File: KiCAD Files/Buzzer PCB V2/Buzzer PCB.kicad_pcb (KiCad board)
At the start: 2 copper layers, 90 x 50 mm, 18 parts, among them J1 2600mAh LiPo JST-PH bottom, J10 Adafruit ESP32 Feather V2 hea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, J11 OLED FeatherWing header, J2 Legacy SW_BAT/GND out, J3 SD card module, swapped pins, J4 Legacy D13 test pad, J5 GPS M100 Mini, J6 BMP390/BMP5xx top module, J7 SHT41 top module, Q1 S8050, SW1 SS12D00G5, U1 TP4057 USB-C charger

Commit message: V2 with sparkfun
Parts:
- added SW2: BACK, Vario_Buzzer_V2:Ant_Display_SW_PUSH_6mm_H5mm, F.Cu at (4.00, 41.0)
- added SW3: NEXT, Vario_Buzzer_V2:Ant_Display_SW_PUSH_6mm_H5mm, F.Cu at (14.0, 41.0)
- added SW4: DOWN, Vario_Buzzer_V2:Ant_Display_SW_PUSH_6mm_H5mm, F.Cu at (24.0, 41.0)
- added SW5: UP, Vario_Buzzer_V2:Ant_Display_SW_PUSH_6mm_H5mm, F.Cu at (38.0, 41.0)
- J10: value Adafruit ESP32 Feather V2 header -> SparkFun Thing Plus ESP32 WROOM-C USB-C header; footprint Vario_Buzzer_V2:Feather_28_Header_Separate -> Vario_Buzzer_V2:SparkFun_Thing_Plus_ESP32_WROOM_C_Header
- J11: value OLED FeatherWing header -> SparkFun Qwiic OLED 1.3in module; footprint Vario_Buzzer_V2:OLED_FeatherWing_28_Header -> Vario_Buzzer_V2:SparkFun_Qwiic_OLED_1p3_Module
- J3: value SD card module, swapped pins -> Optional external SD module; Thing Plus has onboard microSD
- J5: value GPS M100 Mini -> HGLRC M100 Mini GPS manual pinout
- J6: value BMP390/BMP5xx top module -> BMP390/BMP5xx top pads
- J7: value SHT41 top module -> SHT41 top pads
- moved U1 72.0 mm to (10.5, 6.80), turned to 180 degrees
- moved C2 40.7 mm to (18.2, 9.50)
- moved C1 36.0 mm to (22.5, 4.20)
- moved SW1 32.5 mm to (25.0, 12.0)
- moved J10 32.0 mm to (60.0, 13.0)
- moved J4 17.9 mm to (68.0, 15.0)
- moved BZ1 17.5 mm to (85.0, 13.0)
- moved J7 15.3 mm to (81.0, 37.0), turned to 90 degrees
- moved J5 15.3 mm to (72.0, 41.5)
- moved J3 12.9 mm to (52.0, 31.0)
- moved J11 11.4 mm to (18.0, 31.6)
- moved R1 10.7 mm to (70.5, 15.0)
- moved J6 7.94 mm to (61.0, 35.0)
- moved R2 5.73 mm to (74.0, 15.0)
- moved Q1 4.92 mm to (78.0, 15.0)
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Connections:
- J10 pad 1: RESET -> SDA
- J10 pad 11: SPI_SCK -> (no net)
- J10 pad 12: SPI_MOSI -> SW_BAT
- J10 pad 13: SPI_MISO -> BTN_UP_GPIO21
- J10 pad 14: GPS_TX_FEATHER_RX -> GPS_RX_THING_TX
- J10 pad 15: GPS_RX_FEATHER_TX -> GPS_TX_THING_RX
- J10 pad 16: (no net) -> SPI_MISO
- J10 pad 17: SDA -> SPI_MOSI
- J10 pad 18: SCL -> SPI_SCK
- J10 pad 19: D5_IO14_BTN_C -> (no net)
- J10 pad 2: 3V3 -> SCL
- J10 pad 20: D6_IO32_BTN_B -> (no net)
- J10 pad 21: D9_IO15_BTN_A -> (no net)
- J10 pad 22: SD_CS_D10_IO27 -> (no net)
- J10 pad 25: D13 -> GND
- J10 pad 27: (no net) -> 3V3
- J10 pad 28: SW_BAT -> (no net)
- J10 pad 4: GND -> BTN_DOWN_GPIO5
- J10 pad 5: (no net) -> BTN_NEXT_GPIO4
- J10 pad 6: (no net) -> BTN_BACK_GPIO3
- J10 pad 7: (no net) -> SD_CS_GPIO2
- J10 pad 9: (no net) -> D13_BUZZER_GPIO13
- J11 pad 1: RESET -> GND
- J11 pad 3: (no net) -> SDA
- J11 pad 4: GND -> SCL
- J3 pad 5: SD_CS_D10_IO27 -> SD_CS_GPIO2
- J4 pad e: D13 -> D13_BUZZER_GPIO13
- J5 pad 1: GND -> GPS_RX_THING_TX
- J5 pad 2: 3V3 -> GPS_TX_THING_RX
- J5 pad 3: GPS_TX_FEATHER_RX -> 3V3
- J5 pad 4: GPS_RX_FEATHER_TX -> GND
- R1 pad 1: D13 -> D13_BUZZER_GPIO13
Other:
- board text added: "BTN nets copied from Ant Display: BACK GPIO3, NEXT GPIO4, DOWN GPIO5, UP net on FREEBIE/ESP4"
- board text added: "Back side: optional external SD plus HGLRC M100"
- board text added: "C1 bulk, C2 decoupling on SW_BAT/GND"
- board text added: "J1 bottom LiPo JST"
- board text added: "J10 SparkFun Thing Plus ESP32 WROOM-C, SparkFun Eagle header geometry"
- board text added: "J11 SparkFun Qwiic OLED 1.3in; J3 pins GND 3V3 SDA SCL"
- board text added: "J5 HGLRC M100 manual pin order: RX TX VCC GND"
- board text added: "PCB 90x50mm, 1.5mm FR4; drill set: 0.8/1/1.2/1.4/1.6/2/2.4/3/3.175mm"
- board text added: "R1 470R D13/GPIO13 to Q1 base"
- board text added: "R2 100k base to GND; Q1 S8050 E-B-C"
- board text added: "U1 USB-C edge faces board left; BAT pads face right"
- board text added: "Vario Buzzer / Sensor Interposer V2 - SparkFun Thing Plus + Qwiic OLED, no traces"
- board text removed: "Back: SD + M100"
- board text removed: "C1 47-100uF SW_BAT/GND"
- board text removed: "C2 0.1uF SW_BAT/GND"
- board text removed: "J1 bottom: LiPo JST"
- board text removed: "J10 FEATHER"
- board text removed: "J11 OLED FEATHERWING"
- board text removed: "PCB 90x50mm, 2.0mm"
- board text removed: "Q1 S8050 E-B-C"
- board text removed: "R1 470R D13 to Q1 base"
- board text removed: "R2 100k base to GND"
- board text removed: "U1 USB-C edge -> board edge"
- board text removed: "Vario Buzzer / Sensor Interposer V2 - placement only, no traces"

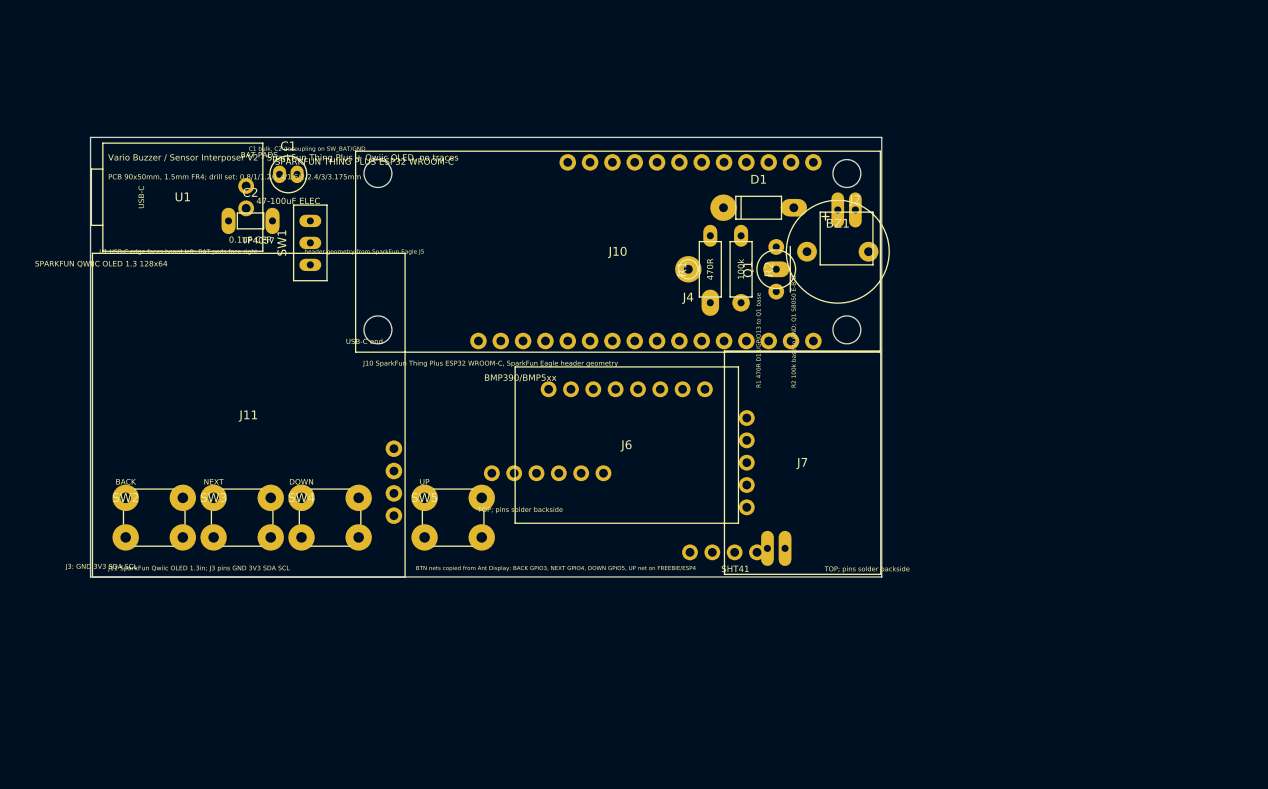
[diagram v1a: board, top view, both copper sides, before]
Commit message: Restore KiCad component references and footprints
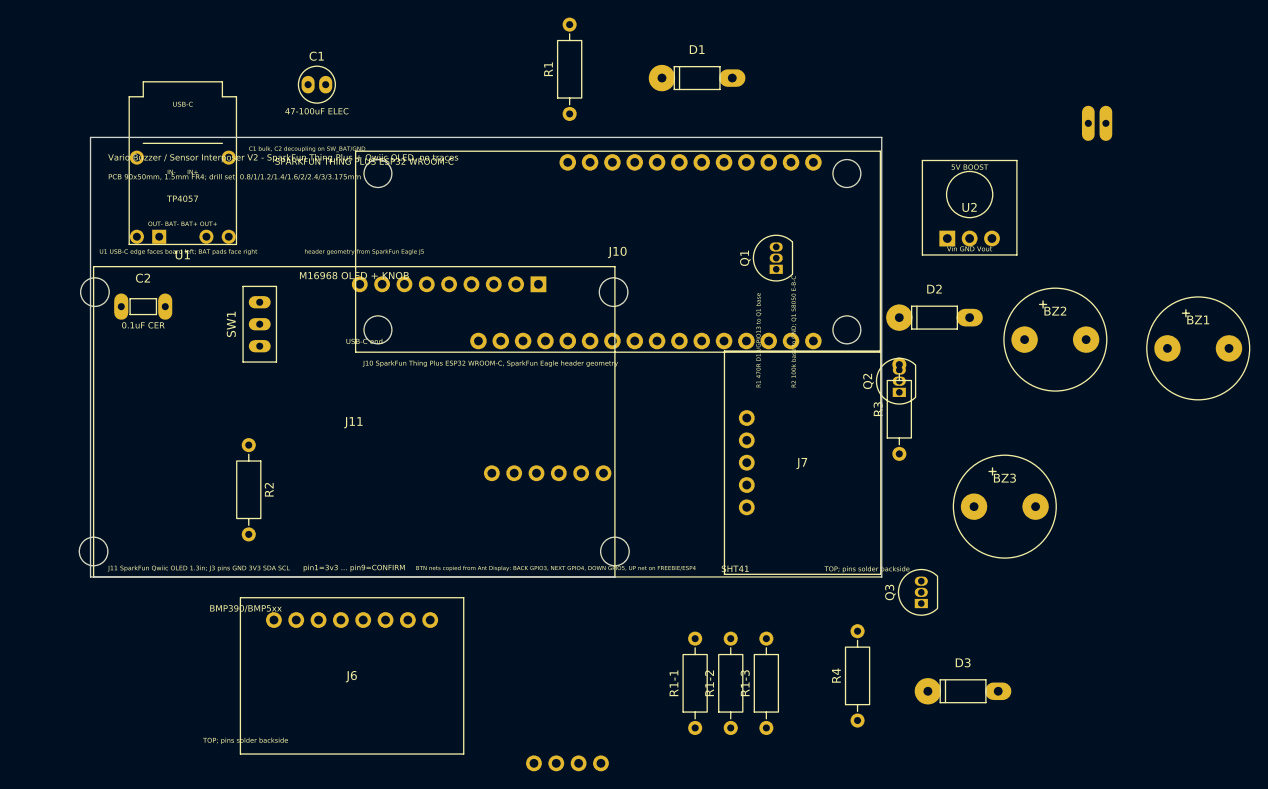
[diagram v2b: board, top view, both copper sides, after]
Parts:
- removed J2: Legacy SW_BAT/GND out, Connector_JST:JST_PH_S2B-PH-K_1x02_P2.00mm_Horizontal
- removed J4: Legacy D13 test pad, Connector_PinHeader_2.54mm:PinHeader_1x01_P2.54mm_Vertical
- removed SW2: BACK, Vario_Buzzer_V2:Ant_Display_SW_PUSH_6mm_H5mm
- removed SW3: NEXT, Vario_Buzzer_V2:Ant_Display_SW_PUSH_6mm_H5mm
- removed SW4: DOWN, Vario_Buzzer_V2:Ant_Display_SW_PUSH_6mm_H5mm
- removed SW5: UP, Vario_Buzzer_V2:Ant_Display_SW_PUSH_6mm_H5mm
- added BZ2: 12085 Passive Buzzer 42R, Buzzer_Beeper:Buzzer_12x8.5mm_P7.62mm_Custom, F.Cu at (109.8, 23.0)
- added BZ3: 12085 Passive Buzzer 42R, Buzzer_Beeper:Buzzer_12x8.5mm_P7.62mm_Custom, F.Cu at (104.0, 42.0)
- added D2: 1N5819, Diode_THT:D_DO-41_SOD81_P10.16mm_Horizontal, F.Cu at (96.0, 20.5)
- added D3: 1N5819, Diode_THT:D_DO-41_SOD81_P10.16mm_Horizontal, F.Cu at (99.2, 63.0)
- added Q2: S8050, Package_TO_SOT_THT:TO-92_Inline, F.Cu at (92.0, 29.0)
- added Q3: S8050, Package_TO_SOT_THT:TO-92_Inline, F.Cu at (94.5, 53.0)
- added R1-1: 100k, Resistor_THT:R_Axial_DIN0207_L6.3mm_D2.5mm_P10.16mm_Horizontal, F.Cu at (68.8, 67.2)
- added R1-2: 100k, Resistor_THT:R_Axial_DIN0207_L6.3mm_D2.5mm_P10.16mm_Horizontal, F.Cu at (72.8, 67.2)
- added R1-3: 100k, Resistor_THT:R_Axial_DIN0207_L6.3mm_D2.5mm_P10.16mm_Horizontal, F.Cu at (76.9, 67.2)
- added R3: 470R, Resistor_THT:R_Axial_DIN0207_L6.3mm_D2.5mm_P10.16mm_Horizontal, F.Cu at (92.0, 36.0)
- added R4: 470R, Resistor_THT:R_Axial_DIN0207_L6.3mm_D2.5mm_P10.16mm_Horizontal, F.Cu at (87.2, 66.3)
- added U2: Comidox 5V Booster, Vario_Buzzer_V2:Comidox_5V_Booster_10.75x10.75_3Pin, F.Cu at (100.0, 8.00)
- C2: footprint Capacitor_THT:C_Disc_D3.0mm_W1.6mm_P2.50mm -> Vario_Buzzer_V2:Ceramic_Cap_0.1uF_P5.00mm_V1
- J10: value SparkFun Thing Plus ESP32 WROOM-C USB-C header -> SparkFun Thing Plus ESP32 WROOM-C USB-C
- J11: value SparkFun Qwiic OLED 1.3in module -> M16968 OLED + Rotary Knob; footprint Vario_Buzzer_V2:SparkFun_Qwiic_OLED_1p3_Module -> Vario_Buzzer_V2:OLED_M16968_59x35_9Pin
- J3: value Optional external SD module; Thing Plus has onboard microSD -> Optional SD module 18x18 swapped
- J5: value HGLRC M100 Mini GPS manual pinout -> HGLRC M100 Mini GPS
- J6: value BMP390/BMP5xx top pads -> BMP581/BMP5xx top pads
- Q1: footprint Package_TO_SOT_THT:TO-92_Inline_Wide_Formed -> Package_TO_SOT_THT:TO-92_Inline
- R1: footprint Resistor_THT:R_Axial_DIN0207_L6.3mm_D2.5mm_P7.62mm_Horizontal -> Resistor_THT:R_Axial_DIN0207_L6.3mm_D2.5mm_P10.16mm_Horizontal
- R2: value 100k -> 470R; footprint Resistor_THT:R_Axial_DIN0207_L6.3mm_D2.5mm_P7.62mm_Horizontal -> Resistor_THT:R_Axial_DIN0207_L6.3mm_D2.5mm_P10.16mm_Horizontal
- SW1: value SS12D00G5 -> SS12D00G5 power switch
- U1: footprint Vario_Buzzer_V2:TP4057_Module_18.2x12.3 -> Vario_Buzzer_V2:TP4057_Module_12.2x18.5
- moved J1 60.6 mm to (114.5, -3.35)
- moved R2 59.5 mm to (18.0, 35.0)
- moved BZ1 42.4 mm to (126.0, 24.0)
- moved J6 40.8 mm to (29.8, 61.2)
- moved J5 29.9 mm to (54.2, 65.5)
- moved R1 23.8 mm to (54.5, -2.67)
- moved D1 16.3 mm to (69.0, -6.75)
- moved C2 15.6 mm to (6.00, 19.2)
- moved J11 12.0 mm to (30.0, 32.4)
- moved SW1 10.9 mm to (19.2, 21.2)
- moved C1 10.7 mm to (25.8, -6.00)
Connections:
- BZ1 pad 1: SW_BAT -> /BUZZER_LOW
- BZ1 pad 2: BUZZER_LOW -> /A
- C1 pad 1: SW_BAT -> /GND
- C1 pad 2: GND -> /SW_BAT
- C2 pad 1: SW_BAT -> /GND
- C2 pad 2: GND -> unconnected-(C2-Pad2)
- D1 pad 1: SW_BAT -> /BUZZER_LOW
- D1 pad 2: BUZZER_LOW -> /A
- J1 pad 1: BAT_IN -> /GND
- J1 pad 2: GND -> /BAT_IN
- J10 pad 1: SDA -> /SDA
- J10 pad 10: (no net) -> unconnected-(J10-V_USB-Pad10)
- J10 pad 11: (no net) -> unconnected-(J10-EN-Pad11)
- J10 pad 12: SW_BAT -> /SW_BAT
- J10 pad 13: BTN_UP_GPIO21 -> unconnected-(J10-FREEBIE/ESP4-Pad13)
- J10 pad 14: GPS_RX_THING_TX -> /GPS_RX_THING_TX
- J10 pad 15: GPS_TX_THING_RX -> /D13_BUZZER_GPIO13
- J10 pad 16: SPI_MISO -> /SPI_MISO
- J10 pad 17: SPI_MOSI -> /SPI_MOSI
- J10 pad 18: SPI_SCK -> /SPI_SCK
- J10 pad 19: (no net) -> /BTN_BACK_GPIO3
- J10 pad 2: SCL -> /SCL
- J10 pad 20: (no net) -> /BTN_NEXT_GPIO4
- J10 pad 21: (no net) -> /BTN_DOWN_GPIO5
- J10 pad 22: (no net) -> /BTN_UP_GPIO21
- J10 pad 23: (no net) -> /SD_CS_GPIO2
- J10 pad 24: (no net) -> /BUZZER2_ESP26
- J10 pad 25: GND -> /GND
- J10 pad 26: (no net) -> unconnected-(J10-AREF/NC-Pad26)
- J10 pad 27: 3V3 -> unconnected-(J10-3V3-Pad27)
- J10 pad 28: (no net) -> unconnected-(J10-RESET-Pad28)
- J10 pad 3: (no net) -> unconnected-(J10-GPIO6/ESP14-Pad3)
- J10 pad 4: BTN_DOWN_GPIO5 -> unconnected-(J10-GPIO5/ESP32-Pad4)
- J10 pad 5: BTN_NEXT_GPIO4 -> unconnected-(J10-GPIO4/ESP15-Pad5)
- J10 pad 6: BTN_BACK_GPIO3 -> unconnected-(J10-GPIO3/ESP33-Pad6)
- J10 pad 7: SD_CS_GPIO2 -> /BUZZER3_GPIO2_ESP27
- J10 pad 8: (no net) -> unconnected-(J10-GPIO1/ESP12-Pad8)
- J10 pad 9: D13_BUZZER_GPIO13 -> /GPS_TX_THING_RX
- J11 pad 1: GND -> /3V3
- J11 pad 2: 3V3 -> /GND
- J11 pad 3: SDA -> /BTN_BACK_GPIO3
- J11 pad 4: SCL -> /BTN_NEXT_GPIO4
- J3 pad 1: GND -> /3V3
- J3 pad 2: SPI_MISO -> /SD_CS_GPIO2
- J3 pad 3: SPI_SCK -> /SPI_MOSI
- J3 pad 4: SPI_MOSI -> /SPI_SCK
- J3 pad 5: SD_CS_GPIO2 -> /SPI_MISO
- J3 pad 6: 3V3 -> /GND
- J5 pad 1: GPS_RX_THING_TX -> /GND
- J5 pad 2: GPS_TX_THING_RX -> /3V3
- J5 pad 3: 3V3 -> /GPS_TX_THING_RX
- J5 pad 4: GND -> /GPS_RX_THING_TX
- J6 pad 1: 3V3 -> /3V3
- J6 pad 2: 3V3 -> /3V3
- J6 pad 3: GND -> /GND
- J6 pad 4: SCL -> /SCL
- J6 pad 5: (no net) -> unconnected-(J6-SDO/ADR-Pad5)
- J6 pad 6: SDA -> /SDA
- J6 pad 7: (no net) -> unconnected-(J6-CS-Pad7)
- J6 pad 8: (no net) -> unconnected-(J6-INT-Pad8)
- J7 pad 1: 3V3 -> /3V3
- J7 pad 2: 3V3 -> /3V3
- J7 pad 3: GND -> /GND
- J7 pad 4: SCL -> /SCL
- J7 pad 5: SDA -> /SDA
- Q1 pad 1: GND -> /BUZZER_LOW
- Q1 pad 2: BUZZER_BASE -> /BUZZER_BASE
- Q1 pad 3: BUZZER_LOW -> /GND
- R1 pad 1: D13_BUZZER_GPIO13 -> /BUZZER_BASE
- R1 pad 2: BUZZER_BASE -> /D13_BUZZER_GPIO13
- R2 pad 1: BUZZER_BASE -> /BUZZER_BASE2
- R2 pad 2: GND -> /BUZZER2_ESP26
- SW1 pad 1: SW_BAT -> /GND
- SW1 pad 2: BAT_IN -> /BAT_IN
- SW1 pad 3: (no net) -> /SW_BAT
- U1 pad 1: BAT_IN -> /GND
- U1 pad 2: GND -> /BAT_IN

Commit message: Reposition buzzer PCB footprints and add SHT41 header
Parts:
- moved R2 214.1 mm to (231.2, 54.5), turned to 180 degrees
- moved D1 192.7 mm to (259.2, 24.5)
- moved R1 180.5 mm to (231.2, 34.5), turned to 180 degrees
- moved R1-1 180.0 mm to (247.2, 43.4)
- moved R1-2 174.4 mm to (247.2, 63.4)
- moved R1-3 171.1 mm to (247.2, 83.4)
- moved D2 164.9 mm to (259.2, 44.5)
- moved Q1 161.3 mm to (238.2, 34.5)
- moved D3 159.9 mm to (259.2, 64.5)
- moved BZ3 158.5 mm to (259.2, 74.5)
- moved BZ2 152.7 mm to (259.2, 54.5)
- moved Q2 148.4 mm to (238.2, 54.5)
- moved Q3 145.3 mm to (238.2, 74.5)
- moved R4 145.1 mm to (231.2, 84.5), turned to 180 degrees
- moved R3 144.4 mm to (231.2, 74.5), turned to 180 degrees
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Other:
- board outline removed

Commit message: asd
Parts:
- removed R4: 470R, Resistor_THT:R_Axial_DIN0207_L6.3mm_D2.5mm_P10.16mm_Horizontal
- R1, R1-1, R1-2, R1-3, R2, R3: moved to B.Cu
- moved R2 117.3 mm to (115.3, 72.8), turned to 0 degrees
- moved R3 103.5 mm to (128.3, 63.0), turned to 0 degrees
- moved R1 100.1 mm to (138.5, 72.5)
- moved J5 74.5 mm to (151.5, 76.0), turned to -90 degrees
- moved R1-3 73.7 mm to (177.9, 58.0), turned to 0 degrees
- moved SW1 70.9 mm to (52.0, 113.8)
- moved R1-2 70.6 mm to (178.0, 49.0), turned to 0 degrees
- moved R1-1 69.7 mm to (177.5, 40.5), turned to 0 degrees
- moved U2 61.8 mm to (165.2, 34.7), turned to 90 degrees
- moved D1 61.3 mm to (198.6, 34.0), turned to 90 degrees
- moved Q3 50.0 mm to (191.4, 56.7), turned to -90 degrees
- moved BZ2 48.7 mm to (210.8, 49.2), turned to 90 degrees
- moved BZ1 48.4 mm to (210.8, 33.8), turned to 90 degrees
- moved Q2 47.2 mm to (191.5, 47.7), turned to -90 degrees
- moved Q1 46.8 mm to (191.6, 39.2), turned to -90 degrees
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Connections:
- J10 pad 13: unconnected-(J10-FREEBIE/ESP4-Pad13) -> /OLED_CONFIRM
- J6 pad 2: /3V3 -> unconnected-(J6-3V3-Pad2)
- J7 pad 2: /3V3 -> unconnected-(J7-3V3-Pad2)
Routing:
- net /GND: track 0.00 -> 93.3 mm
- net /A: track 0.00 -> 30.8 mm
- net /SCL: track 0.00 -> 20.2 mm
- net /3V3: track 0.00 -> 20.2 mm
- net /SDA: track 0.00 -> 19.1 mm
- net /BUZZER_LOW: track 0.00 -> 7.01 mm
- net /D13_BUZZER_GPIO13: track 0.00 -> 6.14 mm
- net /BUZZER_BASE: track 0.00 -> 3.93 mm
- net /BUZZER_BASE2: track 0.00 -> 3.36 mm
- net /BUZZER_BASE3: track 0.00 -> 3.31 mm

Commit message: pcb
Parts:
- J3, R1, R1-1, R1-2, R1-3, R2, R3: moved to F.Cu
- moved J3 91.8 mm to (179.5, 112.0), turned to 180 degrees
- moved U1 67.6 mm to (71.3, 107.8), turned to 0 degrees
- moved Q1 62.8 mm to (172.5, 99.0), turned to 0 degrees
- moved BZ1 60.8 mm to (166.2, 75.2), turned to -90 degrees
- moved D1 58.7 mm to (173.5, 87.0), turned to -90 degrees
- moved D2 56.7 mm to (181.2, 87.2), turned to -90 degrees
- moved BZ3 53.9 mm to (191.0, 75.0), turned to -90 degrees
- moved Q2 52.6 mm to (180.0, 99.0), turned to 0 degrees
- moved J1 49.2 mm to (68.6, 82.5), turned to 90 degrees
- moved D3 48.6 mm to (188.2, 87.5), turned to -90 degrees
- moved Q3 42.4 mm to (188.2, 99.0), turned to 0 degrees
- moved BZ2 41.3 mm to (178.5, 75.0), turned to -90 degrees
- moved U2 31.5 mm to (149.5, 62.0), turned to 180 degrees
- moved C1 28.9 mm to (77.0, 82.0), turned to -90 degrees
- moved SW1 24.1 mm to (69.5, 97.2), turned to 0 degrees
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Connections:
- BZ1 pad 1: /BUZZER_LOW -> /BOOST_5V
- BZ1 pad 2: /A -> /BUZZER_LOW
- BZ2 pad 1: /BUZZER_LOW -> /BOOST_5V
- BZ2 pad 2: /A -> /BUZZER_LOW2
- BZ3 pad 1: /BUZZER_LOW -> /BOOST_5V
- BZ3 pad 2: /A -> /BUZZER_LOW3
- C2 pad 2: unconnected-(C2-Pad2) -> /3V3
- D1 pad 1: /BUZZER_LOW -> /BOOST_5V
- D1 pad 2: /A -> /BUZZER_LOW
- D2 pad 1: /BUZZER_LOW -> /BOOST_5V
- D2 pad 2: /A -> /BUZZER_LOW2
- D3 pad 1: /BUZZER_LOW -> /BOOST_5V
- D3 pad 2: /A -> /BUZZER_LOW3
- J1 pad 1: /GND -> /BAT_IN
- J1 pad 2: /BAT_IN -> /GND
- J10 pad 15: /D13_BUZZER_GPIO13 -> /GPS_TX_THING_RX
- J10 pad 27: unconnected-(J10-3V3-Pad27) -> /3V3
- J10 pad 9: /GPS_TX_THING_RX -> /D13_BUZZER_GPIO13
- J3 pad 1: /3V3 -> /GND
- J3 pad 2: /SD_CS_GPIO2 -> /SPI_MISO
- J3 pad 3: /SPI_MOSI -> /SPI_SCK
- J3 pad 4: /SPI_SCK -> /SPI_MOSI
- J3 pad 5: /SPI_MISO -> /SD_CS_GPIO2
- J3 pad 6: /GND -> /3V3
- J5 pad 1: /GND -> /GPS_RX_THING_TX
- J5 pad 2: /3V3 -> /GPS_TX_THING_RX
- J5 pad 3: /GPS_TX_THING_RX -> /3V3
- J5 pad 4: /GPS_RX_THING_TX -> /GND
- Q1 pad 1: /BUZZER_LOW -> /GND
- Q1 pad 3: /GND -> /BUZZER_LOW
- Q2 pad 1: /BUZZER_LOW -> /GND
- Q2 pad 3: /GND -> /BUZZER_LOW2
- Q3 pad 1: /BUZZER_LOW -> /GND
- Q3 pad 3: /GND -> /BUZZER_LOW3
- SW1 pad 1: /GND -> unconnected-(SW1-ON-Pad1)
- U1 pad 1: /GND -> /BAT_IN
- U1 pad 2: /BAT_IN -> /GND
- U2 pad 3: /A -> /BOOST_5V
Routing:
- net /GND: track 93.3 -> 356.4 mm, vias 0 -> 4
- net /BUZZER_BASE2: track 3.36 -> 207.4 mm
- net /SPI_MISO: track 0.00 -> 167.4 mm
- net /BUZZER_BASE: track 3.93 -> 163.4 mm
- net /SPI_SCK: track 0.00 -> 143.2 mm
- net /SPI_MOSI: track 0.00 -> 138.4 mm, vias 0 -> 2
- net /BUZZER_BASE3: track 3.31 -> 137.2 mm
- net /SCL: track 20.2 -> 145.2 mm
- net /SW_BAT: track 0.00 -> 118.1 mm, vias 0 -> 1
- net /SDA: track 19.1 -> 135.2 mm
- net /BOOST_5V: track 0.00 -> 105.1 mm, vias 0 -> 2
- net /SD_CS_GPIO2: track 0.00 -> 91.1 mm
- net /3V3: track 20.2 -> 109.1 mm, vias 0 -> 3
- net /OLED_CONFIRM: track 0.00 -> 34.6 mm, vias 0 -> 2
- net /A: track 30.8 -> 0.00 mm
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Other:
- board outline added: 147.8 x 93.4 mm

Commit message: updated pcb
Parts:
- removed J3: Optional SD module 18x18 swapped, Vario_Buzzer_V2:SD_Module_18x18_6Pin_Back
- J5: moved to F.Cu
- R1, R1-1, R1-2, R1-3, R2, R3: moved to B.Cu
- moved C2 11.1 mm to (77.8, 95.0), turned to 90 degrees
- moved D1 0.50 mm to (173.5, 87.5)
- moved Q2 0.38 mm to (180.4, 99.0)
- moved BZ2 0.28 mm to (178.6, 75.2)
- moved BZ3 0.25 mm to (191.0, 75.2)
- moved D2 0.25 mm to (181.2, 87.5)
- turned J5 to 90 degrees
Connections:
- J10 pad 16: /SPI_MISO -> unconnected-(J10-MISO/POCI_ESP19-Pad16)
- J10 pad 17: /SPI_MOSI -> unconnected-(J10-MOSI/PICO_ESP23-Pad17)
- J10 pad 18: /SPI_SCK -> unconnected-(J10-SCK_ESP18-Pad18)
- J10 pad 23: /SD_CS_GPIO2 -> unconnected-(J10-A1/ESP25-Pad23)
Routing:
- net /SPI_MISO: track 167.4 -> 0.00 mm
- net /SPI_SCK: track 143.2 -> 0.00 mm
- net /GND: track 356.4 -> 496.4 mm, vias 4 -> 1
- net /SPI_MOSI: track 138.4 -> 0.00 mm, vias 2 -> 0
- net /3V3: track 109.1 -> 202.1 mm, vias 3 -> 2
- net /SD_CS_GPIO2: track 91.1 -> 0.00 mm
- net /SCL: track 145.2 -> 67.5 mm
- net /SDA: track 135.2 -> 64.4 mm
- net /SW_BAT: track 118.1 -> 171.6 mm
- net /BUZZER_BASE2: track 207.4 -> 181.8 mm
- net /GPS_TX_THING_RX: track 23.5 -> 0.15 mm
- net /GPS_RX_THING_TX: track 21.7 -> 0.00 mm
- net /BOOST_5V: track 105.1 -> 94.1 mm
- net /BUZZER_BASE: track 163.4 -> 168.0 mm
- net /BUZZER_BASE3: track 137.2 -> 140.3 mm

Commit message: final routing
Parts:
- added ?: , , F.Cu at (133.2, 82.0)
- added ?: , , F.Cu at (149.4, 54.4)
- added ?: , , F.Cu at (89.8, 84.2)
- added ?: , , F.Cu at (145.5, 54.4)
- added REF**: SolderWire-0.127sqmm_1x01_D0.48mm_OD1mm, Connector_Wire:SolderWire-0.127sqmm_1x01_D0.48mm_OD1mm, F.Cu at (153.5, 54.2)
- moved J11 37.0 mm to (78.1, 85.8)
- moved R3 1.50 mm to (128.3, 52.2)
- moved R1 1.25 mm to (123.0, 63.2)
- moved J7 0.13 mm to (156.5, 112.2)
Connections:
- U2 pad 1: /SW_BAT -> /BOOST_5V
- U2 pad 3: /BOOST_5V -> /SW_BAT
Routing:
- net /SDA: track 64.4 -> 181.0 mm
- net /SCL: track 67.5 -> 169.1 mm
- net /GND: track 496.4 -> 422.2 mm, vias 1 -> 0
- net /SW_BAT: track 171.6 -> 115.4 mm
- net /BTN_DOWN_GPIO5: track 12.8 -> 47.8 mm
- net /OLED_CONFIRM: track 34.6 -> 60.9 mm, vias 2 -> 0
- net /GPS_TX_THING_RX: track 0.15 -> 24.7 mm
- net /GPS_RX_THING_TX: track 0.00 -> 20.4 mm
- net /BUZZER2_ESP26: track 27.8 -> 9.58 mm, vias 2 -> 0
- net /3V3: track 202.1 -> 185.7 mm, vias 2 -> 0
- net /BTN_UP_GPIO21: track 12.8 -> 17.0 mm
- net /BTN_NEXT_GPIO4: track 12.8 -> 17.0 mm
- net /BTN_BACK_GPIO3: track 12.8 -> 17.0 mm
- net /BOOST_5V: track 94.1 -> 90.5 mm, vias 2 -> 1
- net /BUZZER3_GPIO2_ESP27: track 4.42 -> 5.92 mm
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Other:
- board size 147.8 x 93.4 mm -> 136.3 x 75.3 mm
